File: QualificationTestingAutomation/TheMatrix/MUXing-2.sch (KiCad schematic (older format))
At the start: 18 parts, among them J17 Banana Jack, U1 DG408LE, U10 MAX14752, U11 MAX14752, U12 MAX14752, U13 MAX14752, U16 DG408LE, U17 DS18B20_, U19 CD74HC4067SM96, U2 DG408LE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

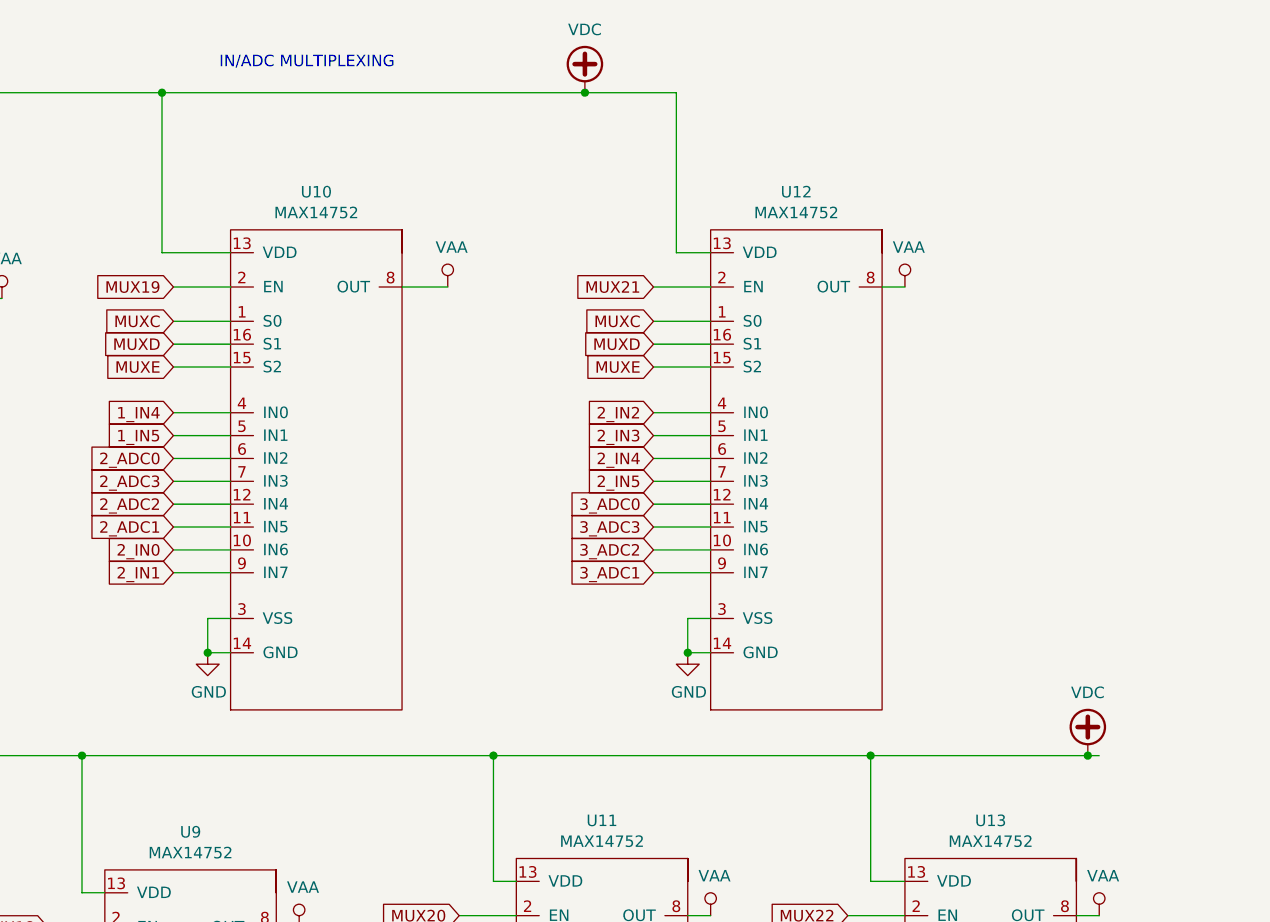
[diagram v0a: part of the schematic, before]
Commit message: Added 60V supply for the MUX's so they can be independent from Vpower, Added another seperate power rail
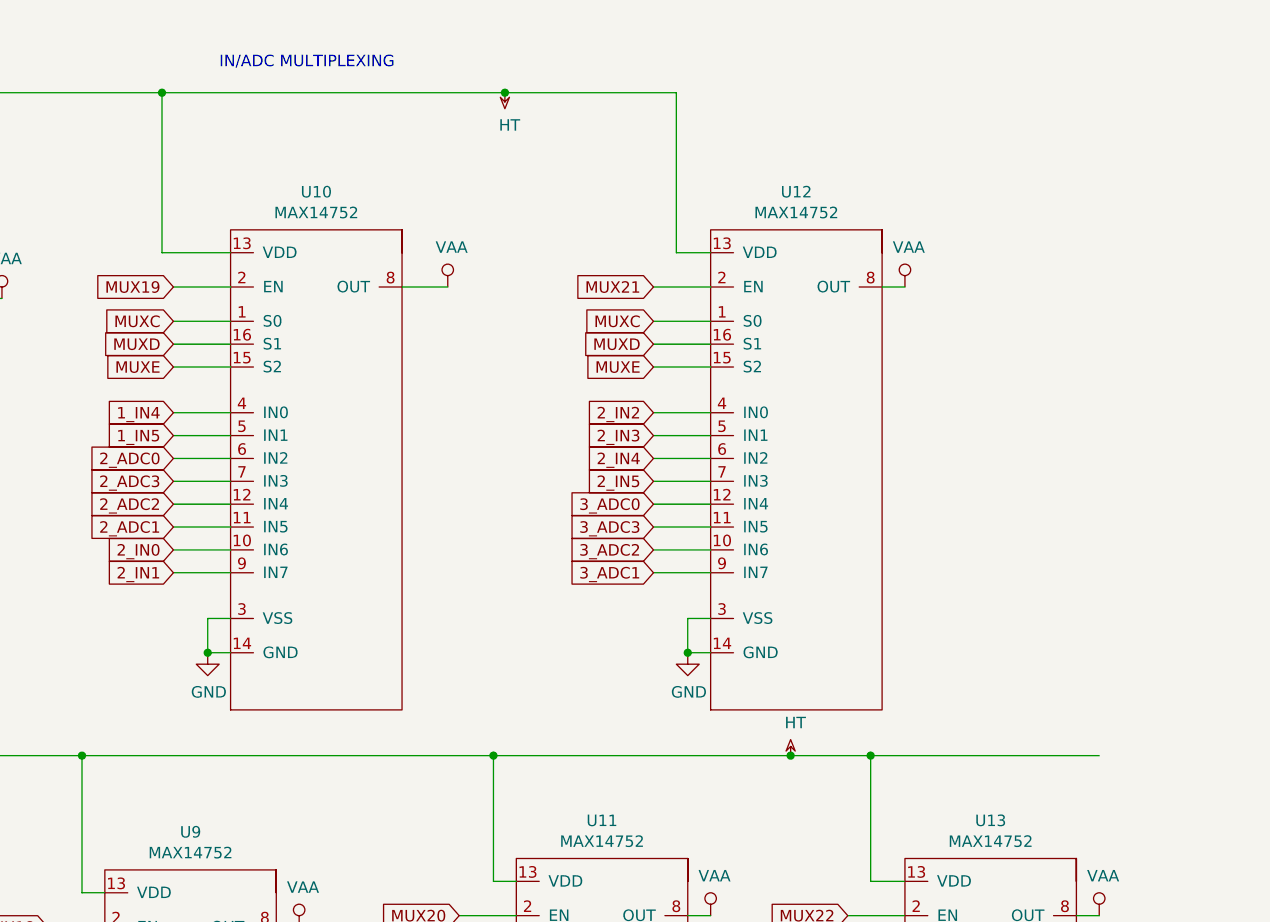
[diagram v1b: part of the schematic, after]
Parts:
- J17: footprint Connectors:Banana_Jack_2Pin -> Connector:Banana_Jack_2Pin_Standard_Spacing
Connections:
- net VDC renamed HT
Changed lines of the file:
@@
 F 0 "J17" H 9980 5792 50  0000 L CNN
 F 1 "Banana Jack" H 9980 5701 50  0000 L CNN
-F 2 "Connectors:Banana_Jack_2Pin" H 9900 5800 50  0001 C CNN
+F 2 "Connector:Banana_Jack_2Pin_Standard_Spacing" H 9900 5800 50  0001 C CNN
 F 3 "~" H 9900 5800 50  0001 C CNN
 F 4 "Multimeter" H 9900 5800 50  0001 C CNN "Field4"
@@
 	5850 2900 5600 2900
 Wire Wire Line
-	3450 1100 5300 1100
-Wire Wire Line
 	1300 4000 3100 4000
 Wire Wire Line
 	3100 4000 4900 4000
-Wire Wire Line
-	4900 4000 6550 4000
-$Comp
-L power:VDC #PWR?
-U 1 1 5C8C561D
-P 7500 4000
-AR Path="/5BA2CD36/5C8C561D" Ref="#PWR?"  Part="1"
-AR Path="/5BCA1CB6/5C8C561D" Ref="#PWR0306"  Part="1"
-F 0 "#PWR0306" H 7500 3900 50  0001 C CNN
-F 1 "VDC" H 7500 4275 50  0000 C CNN
-F 2 "" H 7500 4000 50  0001 C CNN
-F 3 "" H 7500 4000 50  0001 C CNN
-	1    7500 4000
-	1    0    0    -1
-$EndComp
 $Comp
 L power:VAA #PWR0327
@@
 	1    0    0    -1
 $EndComp
-Connection ~ 7500 4000
-Wire Wire Line
-	7500 4000 7550 4000
-Wire Wire Line
-	6550 4000 7500 4000
-$Comp
-L power:VDC #PWR?
-U 1 1 5C905A13
-P 5300 1100
-AR Path="/5BA2CD36/5C905A13" Ref="#PWR?"  Part="1"
-AR Path="/5BCA1CB6/5C905A13" Ref="#PWR0331"  Part="1"
-F 0 "#PWR0331" H 5300 1000 50  0001 C CNN
-F 1 "VDC" H 5300 1375 50  0000 C CNN
-F 2 "" H 5300 1100 50  0001 C CNN
-F 3 "" H 5300 1100 50  0001 C CNN
-	1    5300 1100
-	1    0    0    -1
-$EndComp
 $Comp
 L power:VAA #PWR0332
@@
 Wire Wire Line
 	1600 1100 3450 1100
-Connection ~ 5300 1100
-Wire Wire Line
-	5300 1100 5700 1100
 $Comp
 L TheMatrix-rescue:RESISTOR-passive-SchematicAutomation-rescue R182
@@
 	1    0    0    -1
 $EndComp
+$Comp
+L power:HT #PWR?
+U 1 1 5D5AF49D
+P 4950 1100
+AR Path="/5BA2CD36/5D5AF49D" Ref="#PWR?"  Part="1"
+AR Path="/5BCA1CB6/5D5AF49D" Ref="#PWR0306"  Part="1"
+F 0 "#PWR0306" H 4950 1220 50  0001 C CNN
+F 1 "HT" H 4970 1243 50  0000 C CNN
+F 2 "" H 4950 1100 50  0001 C CNN
+F 3 "" H 4950 1100 50  0001 C CNN
+	1    4950 1100
+	1    0    0    1
+$EndComp
+$Comp
+L power:HT #PWR?
+U 1 1 5D5C0E10
+P 6200 4000
+AR Path="/5BA2CD36/5D5C0E10" Ref="#PWR?"  Part="1"
+AR Path="/5BCA1CB6/5D5C0E10" Ref="#PWR0331"  Part="1"
+F 0 "#PWR0331" H 6200 4120 50  0001 C CNN
+F 1 "HT" H 6220 4143 50  0000 C CNN
+F 2 "" H 6200 4000 50  0001 C CNN
+F 3 "" H 6200 4000 50  0001 C CNN
+	1    6200 4000
+	1    0    0    -1
+$EndComp
+Wire Wire Line
+	6550 4000 7550 4000
+Wire Wire Line
+	3450 1100 4950 1100
+Connection ~ 4950 1100
+Wire Wire Line
+	4950 1100 5700 1100
+Wire Wire Line
+	4900 4000 6200 4000
+Connection ~ 6200 4000
+Wire Wire Line
+	6200 4000 6550 4000
 $EndSCHEMATC
